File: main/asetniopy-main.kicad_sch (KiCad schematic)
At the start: 19 parts, among them J1 Conn_01x02, J2 Conn_01x02, J3 Conn_01x02, J4 Conn_01x02, J5 Conn_01x02, J6 Power/Reset, J7 BAT+, J8 BAT-, U1 ProMicro, U2 LIS2DW12

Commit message: Add LCSC Part numbers for a few parts to test.
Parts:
- C1, C3: LCSC Part # (none) -> C14663
- C2: LCSC Part # (none) -> C7171
- U2: LCSC Part # (none) -> C189624
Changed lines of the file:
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@@
+      (effects (font (size 1.27 1.27)) hide)
+    )
+    (property "LCSC Part #" "C7171" (id 4) (at 116.205 128.27 90)
       (effects (font (size 1.27 1.27)) hide)
     )
@@
       (effects (font (size 1.27 1.27)) hide)
     )
+    (property "LCSC Part #" "C14663" (id 4) (at 116.205 132.08 90)
+      (effects (font (size 1.27 1.27)) hide)
+    )
     (pin "1")
     (pin "2")
@@
       (effects (font (size 1.27 1.27)) hide)
     )
+    (property "LCSC Part #" "C14663" (id 4) (at 108.585 133.35 90)
+      (effects (font (size 1.27 1.27)) hide)
+    )
     (pin "1")
     (pin "2")
@@
       (effects (font (size 1.27 1.27)) hide)
     )
+    (property "LCSC Part #" "C189624" (id 4) (at 111.125 148.59 0)
+      (effects (font (size 1.27 1.27)) hide)
+    )

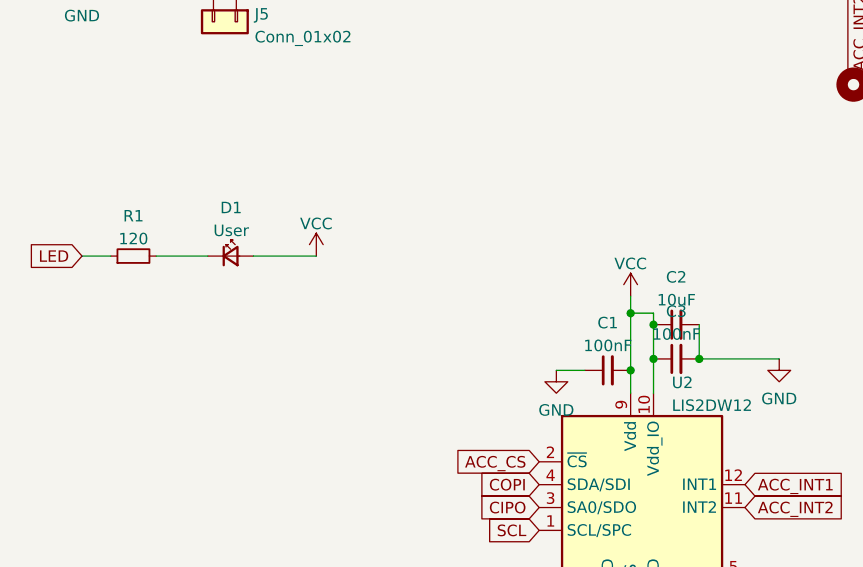
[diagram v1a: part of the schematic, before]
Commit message: More parts, rotation/placement fixes.
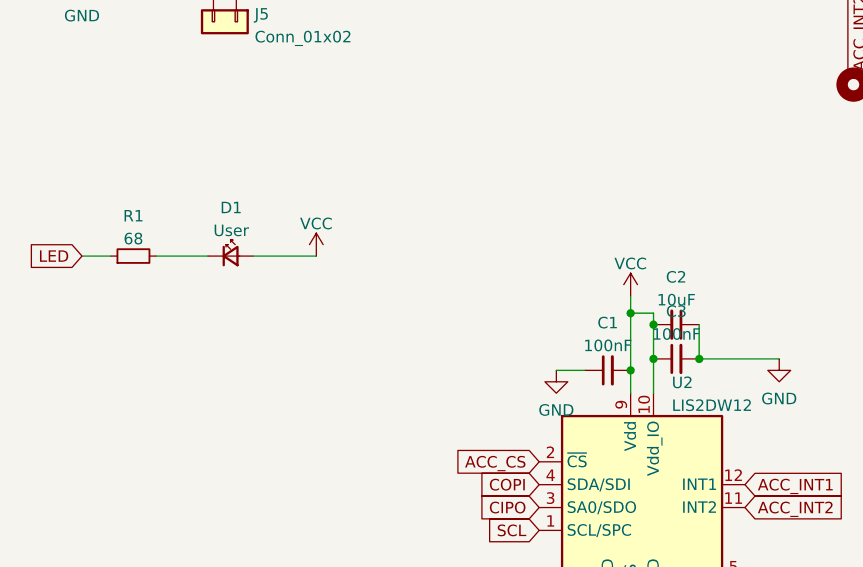
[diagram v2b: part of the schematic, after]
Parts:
- C1, C3: LCSC Part # C14663 -> (none); LCSC Part Number (none) -> C14663
- C2: LCSC Part # C7171 -> (none); LCSC Part Number (none) -> C7171
- D1: LCSC Part Number (none) -> C72041
- R1: value 120 -> 68; LCSC Part Number (none) -> C27592
- U2: LCSC Part # C189624 -> (none); LCSC Part Number (none) -> C189624
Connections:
- net GND: now also C2.1; no longer C2.2
- net VCC: now also C2.2; no longer C2.1
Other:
- moved on the sheet: C2
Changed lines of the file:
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@@
     (in_bom yes) (on_board yes) (fields_autoplaced)
     (property "Reference" "R1" (id 0) (at 55.88 116.2136 90))
-    (property "Value" "120" (id 1) (at 55.88 118.7505 90))
+    (property "Value" "68" (id 1) (at 55.88 118.7505 90))
     (property "Footprint" "Resistor_SMD:R_0603_1608Metric" (id 2) (at 55.88 120.65 0)
       (effects (font (size 1.27 1.27)) hide)
     )
     (property "Datasheet" "~" (id 3) (at 55.88 120.65 0)
+      (effects (font (size 1.27 1.27)) hide)
+    )
+    (property "LCSC Part Number" "C27592" (id 4) (at 55.88 120.65 90)
       (effects (font (size 1.27 1.27)) hide)
     )
@@
     (pin "1")
   )
-  (symbol (lib_id "Device:C_Small") (at 116.205 128.27 90) (unit 1)
-    (in_bom yes) (on_board yes) (fields_autoplaced)
-    (property "Reference" "C2" (id 0) (at 116.2113 123.0081 90))
-    (property "Value" "10uF" (id 1) (at 116.2113 125.545 90))
+  (symbol (lib_id "Device:C_Small") (at 116.205 128.27 270) (mirror x) (unit 1)
+    (in_bom yes) (on_board yes) (fields_autoplaced)
+    (property "Reference" "C2" (id 0) (at 116.1986 123.0081 90))
+    (property "Value" "10uF" (id 1) (at 116.1986 125.545 90))
     (property "Footprint" "Capacitor_Tantalum_SMD:CP_EIA-3216-18_Kemet-A" (id 2) (at 116.205 128.27 0)
       (effects (font (size 1.27 1.27)) hide)
@@
       (effects (font (size 1.27 1.27)) hide)
     )
-    (property "LCSC Part #" "C7171" (id 4) (at 116.205 128.27 90)
+    (property "LCSC Part Number" "C7171" (id 4) (at 116.205 128.27 90)
       (effects (font (size 1.27 1.27)) hide)
     )
@@
       (effects (font (size 1.27 1.27)) hide)
     )
-    (property "LCSC Part #" "C14663" (id 4) (at 116.205 132.08 90)
+    (property "LCSC Part Number" "C14663" (id 4) (at 116.205 132.08 90)
       (effects (font (size 1.27 1.27)) hide)
     )
@@
       (effects (font (size 1.27 1.27)) hide)
     )
+    (property "LCSC Part Number" "C72041" (id 4) (at 66.675 120.65 0)
+      (effects (font (size 1.27 1.27)) hide)
+    )
     (pin "1")
     (pin "2")
@@
       (effects (font (size 1.27 1.27)) hide)
     )
-    (property "LCSC Part #" "C14663" (id 4) (at 108.585 133.35 90)
+    (property "LCSC Part Number" "C14663" (id 4) (at 108.585 133.35 90)
       (effects (font (size 1.27 1.27)) hide)
     )
@@
       (effects (font (size 1.27 1.27)) hide)
     )
-    (property "LCSC Part #" "C189624" (id 4) (at 111.125 148.59 0)
+    (property "LCSC Part Number" "C189624" (id 4) (at 111.125 148.59 0)
       (effects (font (size 1.27 1.27)) hide)
     )
@@
     )
     (path "/01bc0de5-e87e-4cec-88f3-3bef7998270a"
-      (reference "R1") (unit 1) (value "120") (footprint "Resistor_SMD:R_0603_1608Metric")
+      (reference "R1") (unit 1) (value "68") (footprint "Resistor_SMD:R_0603_1608Metric")
     )
     (path "/68a8640f-4b2f-4c4c-a0f5-e46c810f4f86"

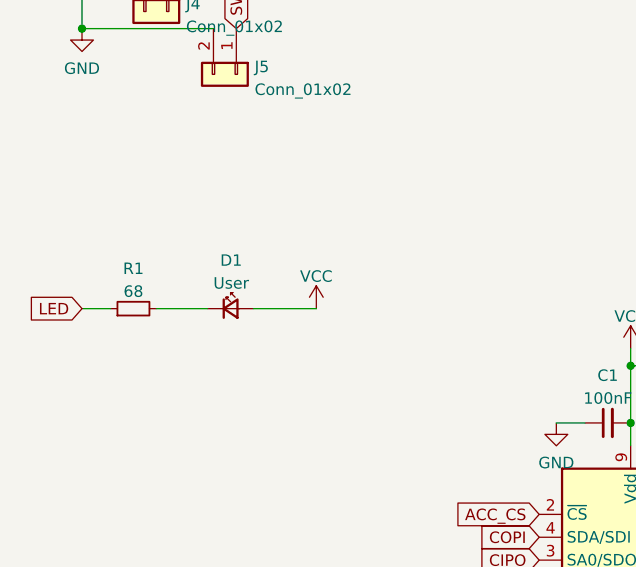
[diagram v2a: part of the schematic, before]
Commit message: Minor placement/silk tweaks.
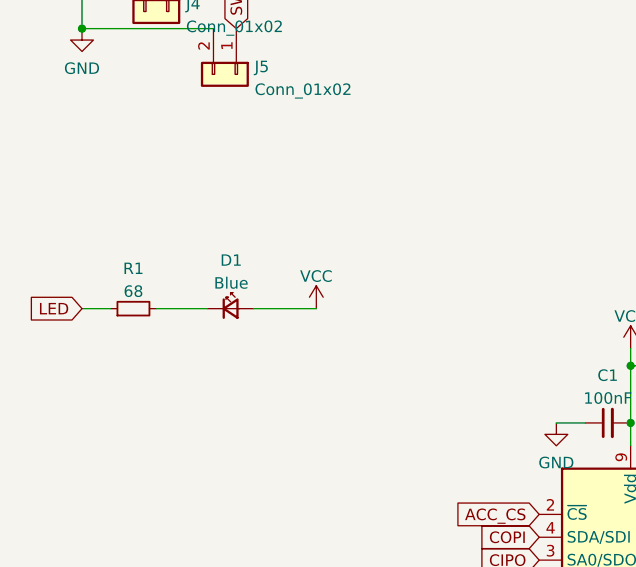
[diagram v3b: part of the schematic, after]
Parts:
- D1: value User -> Blue
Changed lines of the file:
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@@
     (in_bom yes) (on_board yes) (fields_autoplaced)
     (property "Reference" "D1" (id 0) (at 66.7385 115.2992 0))
-    (property "Value" "User" (id 1) (at 66.7385 117.8361 0))
+    (property "Value" "Blue" (id 1) (at 66.7385 117.8361 0))
     (property "Footprint" "LED_SMD:LED_0603_1608Metric" (id 2) (at 66.675 120.65 90)
       (effects (font (size 1.27 1.27)) hide)
@@
     )
     (path "/a3912c3b-a7ed-4069-b82c-93c869bd3701"
-      (reference "D1") (unit 1) (value "User") (footprint "LED_SMD:LED_0603_1608Metric")
+      (reference "D1") (unit 1) (value "Blue") (footprint "LED_SMD:LED_0603_1608Metric")
     )
     (path "/9d3116ed-06f0-4c20-9f12-ed2bc968344c"
